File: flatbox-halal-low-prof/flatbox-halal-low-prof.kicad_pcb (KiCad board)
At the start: 2 copper layers, 230 x 130 mm, 25 parts, among them SW1 SW_Push, SW10 SW_Push, SW11 SW_Push, SW12 SW_Push, SW13 SW_Push, SW14 SW_Push, SW15 SW_Push, SW16 SW_Push, SW17 SW_Push, SW18 SW_Push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

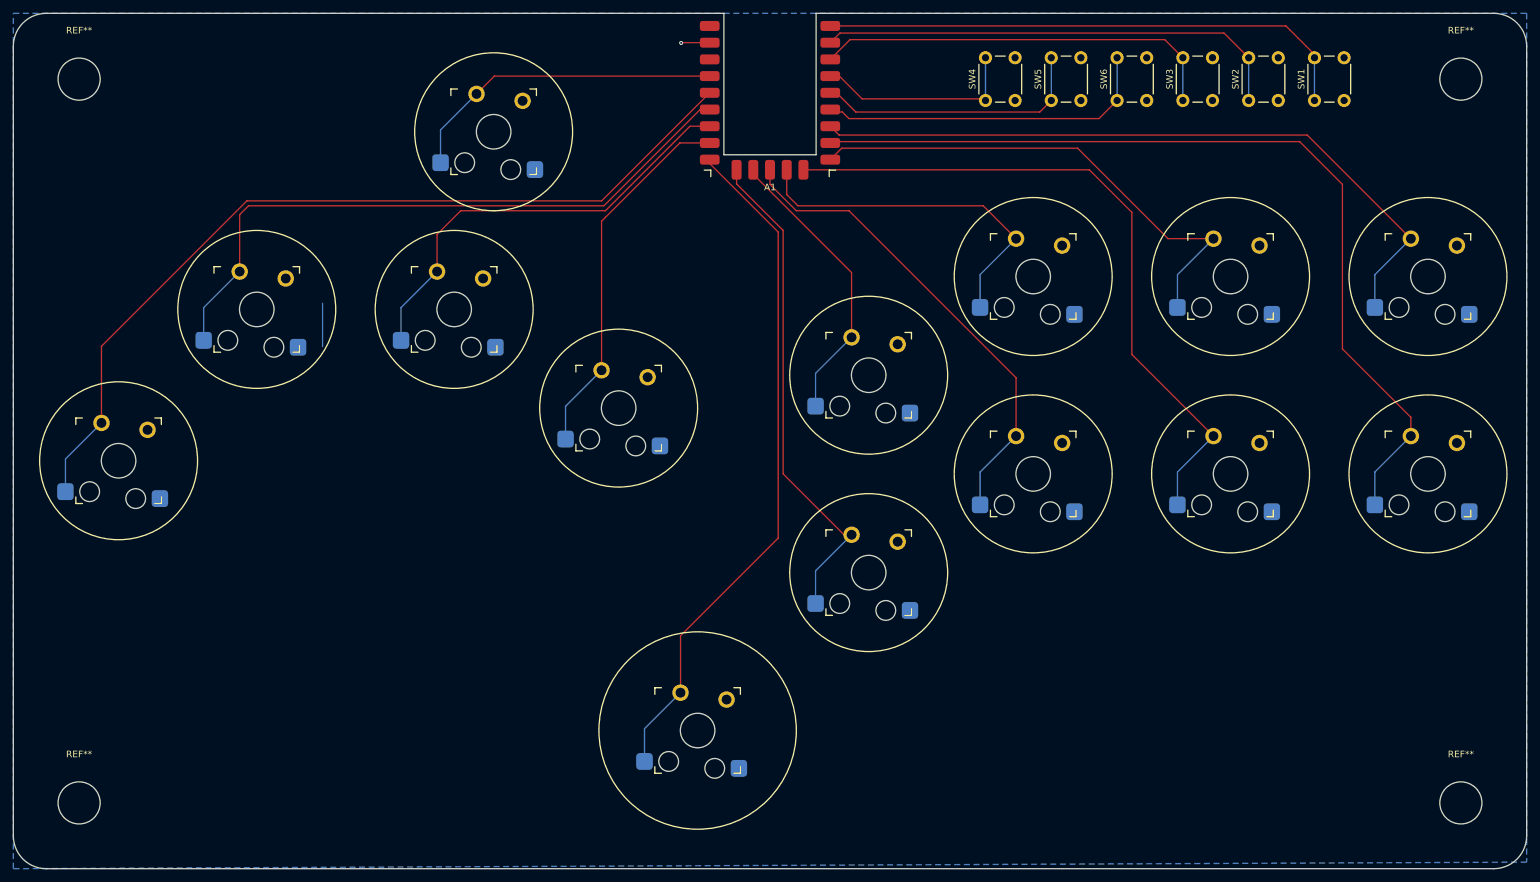
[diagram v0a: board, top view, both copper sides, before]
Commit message: cleaned up signal trace
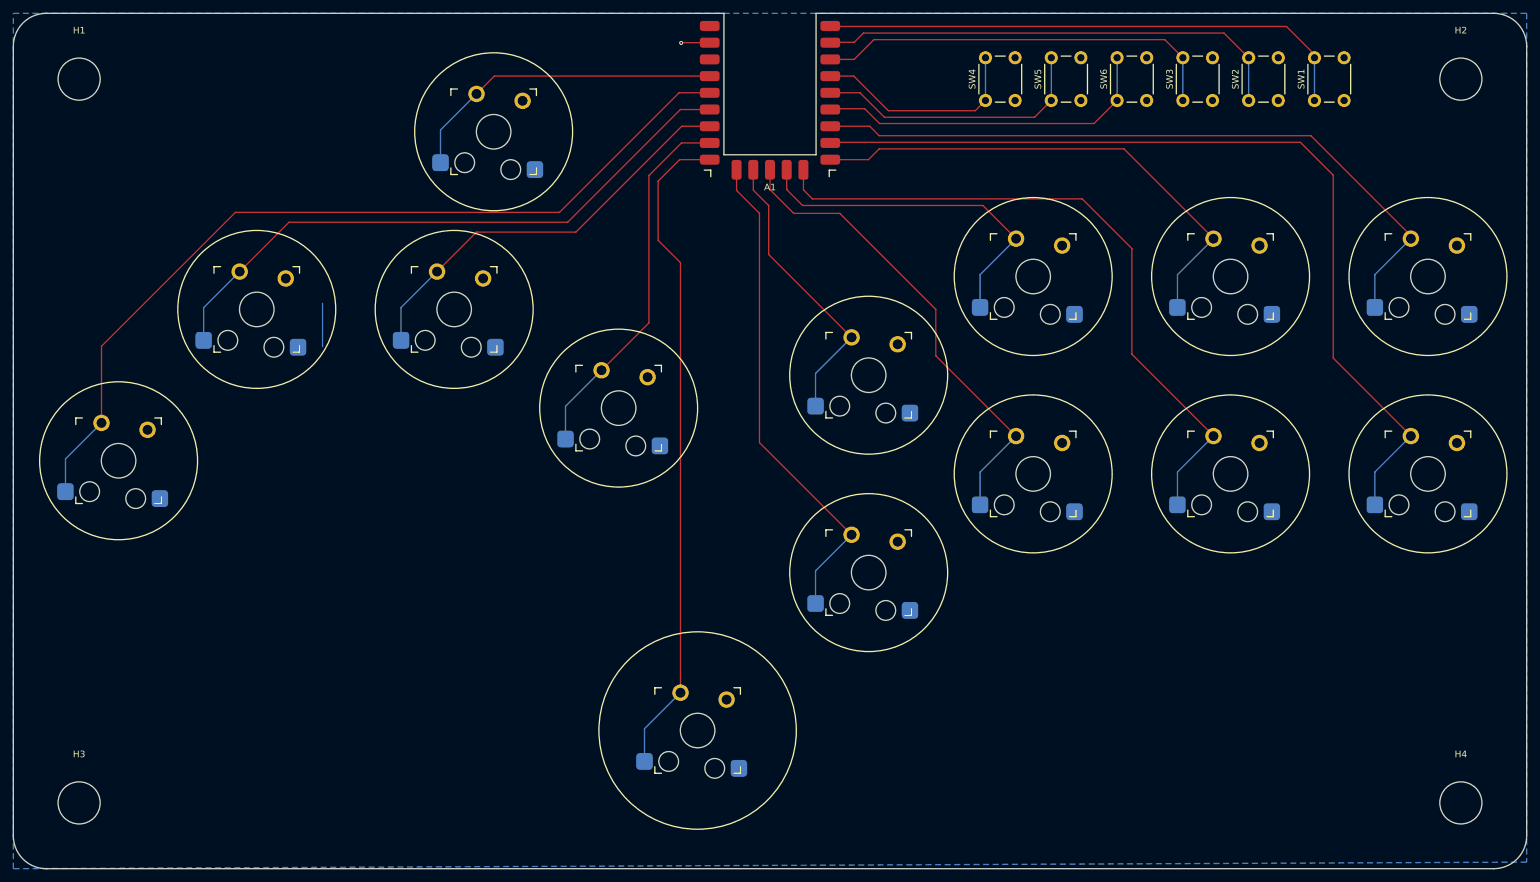
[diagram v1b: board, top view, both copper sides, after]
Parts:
- removed REF** (x4): MountingHole_6.4mm_M6, MountingHole:MountingHole_6.4mm_M6
- added H1: MountingHole, MountingHole:MountingHole_6.4mm_M6, F.Cu at (10.0, 10.0)
- added H2: MountingHole, MountingHole:MountingHole_6.4mm_M6, F.Cu at (220.0, 10.0)
- added H3: MountingHole, MountingHole:MountingHole_6.4mm_M6, F.Cu at (10.0, 120.0)
- added H4: MountingHole, MountingHole:MountingHole_6.4mm_M6, F.Cu at (220.0, 120.0)
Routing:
- net LEFT: track 99.4 -> 94.4 mm
- net DOWN: track 66.6 -> 63.3 mm
- net UP: track 104.2 -> 101.1 mm
- net R2: track 104.5 -> 103.0 mm
- net OPT4: track 31.6 -> 32.9 mm
- net OPT6: track 51.8 -> 52.5 mm
- net OPT5: track 42.0 -> 42.7 mm
- net CROSS: track 76.1 -> 76.7 mm
- net CIRCLE: track 73.4 -> 72.8 mm
